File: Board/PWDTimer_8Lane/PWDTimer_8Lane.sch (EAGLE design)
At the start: 13 parts, among them J1 S3B-XH-A(LF)(SN), J2 S3B-XH-A(LF)(SN), J3 S3B-XH-A(LF)(SN), J4 S3B-XH-A(LF)(SN), J5 S3B-XH-A(LF)(SN), J6 S3B-XH-A(LF)(SN), J7 S3B-XH-A(LF)(SN), J8 S3B-XH-A(LF)(SN), P1 S2B-XH-A(LF)(SN), U1 ESP32-DEVKITC-32D

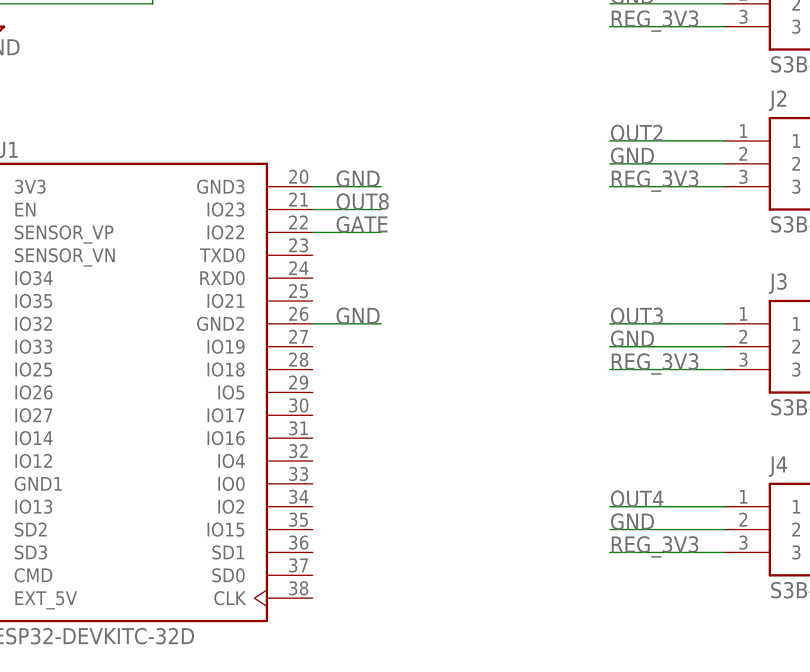
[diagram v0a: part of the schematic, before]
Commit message: Lots of updates to changing how data is stored as a json file, as well as starting the conversion to having groups and racers in the groups instead of just one monolothic racer group.
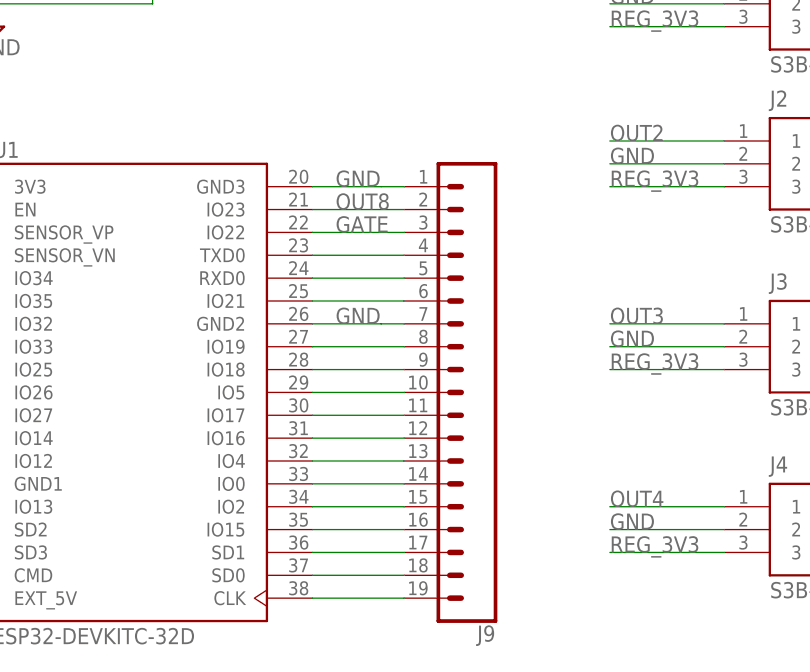
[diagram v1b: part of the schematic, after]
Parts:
- added J9: (no value), SparkFun-Connectors:CONN_191X19_NO_SILK
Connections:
- new net N$1: J9.4, U1.TXD0
- new net N$10: J9.14, U1.IO0
- new net N$11: J9.15, U1.IO2
- new net N$12: J9.16, U1.IO15
- new net N$13: J9.17, U1.SD1
- new net N$14: J9.18, U1.SD0
- new net N$15: J9.19, U1.CLK
- new net N$2: J9.5, U1.RXD0
- new net N$3: J9.6, U1.IO21
- new net N$4: J9.8, U1.IO19
- new net N$5: J9.9, U1.IO18
- new net N$6: J9.10, U1.IO5
- new net N$7: J9.11, U1.IO17
- new net N$8: J9.12, U1.IO16
- new net N$9: J9.13, U1.IO4
- net GATE: now also J9.3
- net GND: now also J9.1, J9.7
- net OUT8: now also J9.2
